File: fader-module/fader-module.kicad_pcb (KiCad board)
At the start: 2 copper layers, 33 parts, among them J1 Conn_1x05_Pin, J2 Conn_1x05_Socket, J7 Conn_01x06_Socket, SW1 1825910-6, SW2 1825910-6, U5 ATMEGA328P-AUR, U7 DRV8871DDAR

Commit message: fader begin route except i forgot widths anyways theyre mostly laid out the components i mean
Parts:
- moved C8 138.6 mm to (209.3, 90.4), turned to 90 degrees
- moved C7 138.5 mm to (209.2, 85.3), turned to -90 degrees
- moved R5 134.8 mm to (215.1, 90.7), turned to -90 degrees
- moved R4 134.8 mm to (215.1, 85.6), turned to -90 degrees
- moved C12 103.1 mm to (176.4, 107.9), turned to -90 degrees
- moved C13 100.7 mm to (176.3, 91.5), turned to -90 degrees
- moved R7 85.0 mm to (165.1, 86.7)
- moved R8 83.6 mm to (162.6, 110.3), turned to 90 degrees
- moved R9 83.1 mm to (163.3, 94.2), turned to 90 degrees
- moved C16 73.6 mm to (147.4, 111.8), turned to 180 degrees
- moved C6 72.2 mm to (142.9, 85.6), turned to 180 degrees
- moved SW1 70.0 mm to (170.0, 110.9)
- moved C11 67.3 mm to (142.6, 89.9), turned to 180 degrees
- moved SW2 65.7 mm to (170.2, 94.4)
- moved R14 61.6 mm to (143.5, 103.1), turned to 180 degrees
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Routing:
- net GND: track 0.00 -> 77.8 mm
- net +3V3: track 0.00 -> 52.5 mm
- net /MUTE: track 0.00 -> 14.9 mm
- net /SOLO: track 0.00 -> 14.1 mm
- net +9V: track 0.00 -> 12.3 mm
- net Net-(U5-PC0(ADC0/PCINT8)): track 0.00 -> 6.07 mm
- net Net-(U5-PC1(ADC1/PCINT9)): track 0.00 -> 5.93 mm
- net Net-(R15-Pad2): track 0.00 -> 4.26 mm
- net Net-(D2-A): track 0.00 -> 3.95 mm
- net Net-(U7-ILIM): track 0.00 -> 3.80 mm
- net Net-(D1-A): track 0.00 -> 3.79 mm
- net /TOUCH: track 0.00 -> 3.73 mm
- net Net-(R14-Pad2): track 0.00 -> 3.08 mm
- added copper zone on F.Cu, net GND

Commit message: HHHHAAAAHHHHH traces AHH
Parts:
- moved R17 8.60 mm to (102.0, 92.3)
- moved R3 7.18 mm to (93.8, 105.9)
- moved C14 7.14 mm to (101.1, 102.3), turned to -90 degrees
- moved C4 7.14 mm to (101.1, 97.0)
- moved C16 6.82 mm to (146.6, 105.0)
- moved R9 6.82 mm to (162.5, 87.5)
- moved SW2 6.82 mm to (169.4, 87.6)
- moved C13 6.82 mm to (175.5, 84.7)
- moved R14 6.82 mm to (142.7, 96.4)
- moved R16 6.82 mm to (133.9, 95.5)
- moved SW1 6.82 mm to (169.2, 104.1)
- moved U7 6.82 mm to (141.3, 90.1)
- moved C12 6.82 mm to (175.6, 101.2)
- moved J1 6.82 mm to (148.2, 108.3)
- moved R15 6.82 mm to (137.6, 96.4)
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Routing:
- net /MOSI: track 0.00 -> 45.5 mm
- net /MISO: track 0.00 -> 37.1 mm
- net /SCK: track 0.00 -> 33.2 mm
- net +3V3: track 52.5 -> 61.7 mm
- net GND: track 77.8 -> 72.0 mm
- net Net-(R15-Pad2): track 4.26 -> 2.74 mm
- net /TOUCH: track 3.73 -> 3.09 mm
- net +9V: track 12.3 -> 11.7 mm
- net (no net): vias 0 -> 1

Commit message: gotta add connector for motor prob LMAO
also do i need 9v caps??
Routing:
- net GND: track 72.0 -> 135.0 mm, vias 0 -> 2
- net Net-(P1-PadT): track 0.00 -> 61.9 mm, vias 0 -> 2
- net /SERVO: track 0.00 -> 59.0 mm
- net +3V3: track 61.7 -> 102.3 mm
- net /LINE: track 0.00 -> 35.3 mm

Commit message: i will combust
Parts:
- removed J7: Conn_01x06_Socket, Connector_IDC:IDC-Header_2x03_P2.54mm_Vertical
- removed P1: ~, PSM01:PSM01-081A_BRN
- added J3: Conn_01x02_Pin, TerminalBlock_Phoenix:TerminalBlock_Phoenix_MKDS-1,5-2-5.08_1x02_P5.08mm_Horizontal, F.Cu at (153.6, 88.3)
- added J4: Conn_01x06_Pin, Connector_IDC:IDC-Header_2x03_P2.54mm_Vertical, F.Cu at (182.4, 102.9)
- added J6: Conn_01x06_Pin, Connector_IDC:IDC-Header_2x03_P2.54mm_Vertical, F.Cu at (96.0, 83.7)
- D1, D2: footprint LED_SMD:LED_0805_2012Metric_Pad1.15x1.40mm_HandSolder -> Connector_Molex:Molex_KK-254_AE-6410-02A_1x02_P2.54mm_Vertical
- moved C7 24.7 mm to (183.9, 87.0), turned to 90 degrees
- moved C8 24.7 mm to (184.0, 91.9)
- moved R4 24.7 mm to (189.8, 87.1)
- moved R5 24.7 mm to (189.8, 92.1)
- moved J2 8.60 mm to (135.8, 38.9)
- moved R7 4.00 mm to (162.2, 82.8)
- moved C12 2.94 mm to (175.6, 104.1)
- moved R8 2.94 mm to (161.7, 106.5)
- moved R9 2.94 mm to (162.5, 90.4)
- moved SW1 2.94 mm to (169.2, 107.0)
- moved SW2 2.94 mm to (169.4, 90.5)
- moved C13 2.94 mm to (175.5, 87.6)
- moved D2 2.63 mm to (169.6, 82.8)
- moved R6 2.06 mm to (162.6, 99.4)
- moved R3 1.39 mm to (95.1, 106.5)
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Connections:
- R3 pad 2: Net-(P1-PadT) -> Net-(U5-PB2(PCINT2/~{SS}/OC1B))
- U5 pad 14: /TOUCH -> Net-(U5-PB2(PCINT2/~{SS}/OC1B))
- U7 pad 6: Net-(U7-OUT1) -> /A
- U7 pad 8: Net-(U7-OUT2) -> /B
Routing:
- net /SCL: track 0.00 -> 150.6 mm, vias 0 -> 1
- net GND: track 135.0 -> 280.0 mm, vias 2 -> 3
- net /SDA: track 0.00 -> 142.4 mm, vias 0 -> 1
- net /S_LED: track 0.00 -> 113.0 mm, vias 0 -> 2
- net +3V3: track 102.3 -> 204.8 mm, vias 0 -> 2
- net /SOLO: track 14.1 -> 111.8 mm, vias 0 -> 2
- net /MUTE: track 14.9 -> 105.7 mm
- net /M_LED: track 0.00 -> 83.2 mm
- net +9V: track 11.7 -> 81.9 mm, vias 0 -> 3
- net Net-(P1-PadT): track 61.9 -> 0.00 mm, vias 2 -> 0
- net /B: track 0.00 -> 48.7 mm
- net /SERVO: track 59.0 -> 19.7 mm
- net /MOTOR1: track 0.00 -> 35.4 mm
- net /MOTOR2: track 0.00 -> 31.4 mm
- net /A: track 0.00 -> 13.5 mm
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
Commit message: eRrOr FrOnT sOlDeR mAsK
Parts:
- moved C9 33.2 mm to (118.4, 109.2)
- moved J6 33.2 mm to (128.3, 91.0)
- moved R17 33.2 mm to (134.3, 99.3)
- moved R3 33.2 mm to (127.4, 113.8)
- moved U5 33.2 mm to (126.1, 106.1)
- moved C10 33.2 mm to (118.6, 104.8)
- moved C14 33.2 mm to (133.4, 109.6)
- moved C4 33.2 mm to (133.4, 104.3)
- moved J2 28.5 mm to (160.0, 53.9)
- moved J4 20.0 mm to (201.0, 110.2)
- moved R8 18.7 mm to (179.0, 113.6)
- moved C7 18.3 mm to (199.6, 96.3)
- moved C8 18.3 mm to (199.7, 101.1)
- moved R4 18.3 mm to (205.5, 96.3)
- moved R5 18.3 mm to (205.5, 101.4)
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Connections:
- U7 pad 10: (no net) -> GND
- U7 pad 11: (no net) -> GND
- U7 pad 12: (no net) -> GND
- U7 pad 13: (no net) -> GND
- U7 pad 14: (no net) -> GND
- U7 pad 15: (no net) -> GND
- U7 pad 16: (no net) -> GND
- U7 pad 17: (no net) -> GND
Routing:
- net /TOUCH: track 0.00 -> 82.9 mm, vias 0 -> 2
- net Net-(U5-PC1(ADC1/PCINT9)): track 8.27 -> 84.1 mm, vias 0 -> 2
- net Net-(U5-PC0(ADC0/PCINT8)): track 11.2 -> 84.5 mm
- net +3V3: track 204.8 -> 247.2 mm, vias 2 -> 3
- net /SCL: track 150.6 -> 116.6 mm
- net /MOTOR1: track 35.4 -> 69.2 mm, vias 0 -> 2
- net /MOTOR2: track 31.4 -> 63.3 mm, vias 0 -> 2
- net /S_LED: track 113.0 -> 81.7 mm
- net /B: track 48.7 -> 19.0 mm
- net /SDA: track 142.4 -> 113.2 mm
- net /MUTE: track 105.7 -> 77.5 mm
- net GND: track 280.0 -> 303.1 mm, vias 3 -> 5
- net /M_LED: track 83.2 -> 60.1 mm
- net /SOLO: track 111.8 -> 96.9 mm
- net /SCK: track 33.2 -> 27.7 mm, vias 0 -> 1
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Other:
- board outline added: 100 x 75 mm

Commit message: done w pcb gerbert time
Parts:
- moved C9 66.4 mm to (142.8, 47.5), turned to 180 degrees
- moved R5 64.1 mm to (150.7, 134.6), turned to 180 degrees
- moved C10 63.9 mm to (147.3, 47.7), turned to 0 degrees
- moved R4 62.8 mm to (155.7, 134.6), turned to 180 degrees
- moved J4 62.5 mm to (141.8, 130.1), turned to -90 degrees
- moved R3 58.3 mm to (138.2, 56.5), turned to 90 degrees
- moved C8 56.1 mm to (150.9, 128.8), turned to 0 degrees
- moved U5 54.7 mm to (145.9, 55.1), turned to -90 degrees
- moved C7 54.5 mm to (155.8, 128.7), turned to 0 degrees
- moved C12 52.9 mm to (138.5, 120.1), turned to 180 degrees
- moved J2 51.9 mm to (198.2, 89.1), turned to -90 degrees
- moved SW1 47.9 mm to (137.1, 114.1), turned to -90 degrees
- moved C14 47.9 mm to (142.5, 62.5), turned to 180 degrees
- moved J6 46.9 mm to (161.0, 57.4), turned to 180 degrees
- moved C4 44.2 mm to (147.7, 62.5), turned to 0 degrees
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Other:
- board size 100 x 75 mm -> 75 x 100 mm
- rule pad_to_mask_clearance: 0 -> 0.05
- board text added: "Desktop Audio Panel Fader Module v1 Project No. 85"

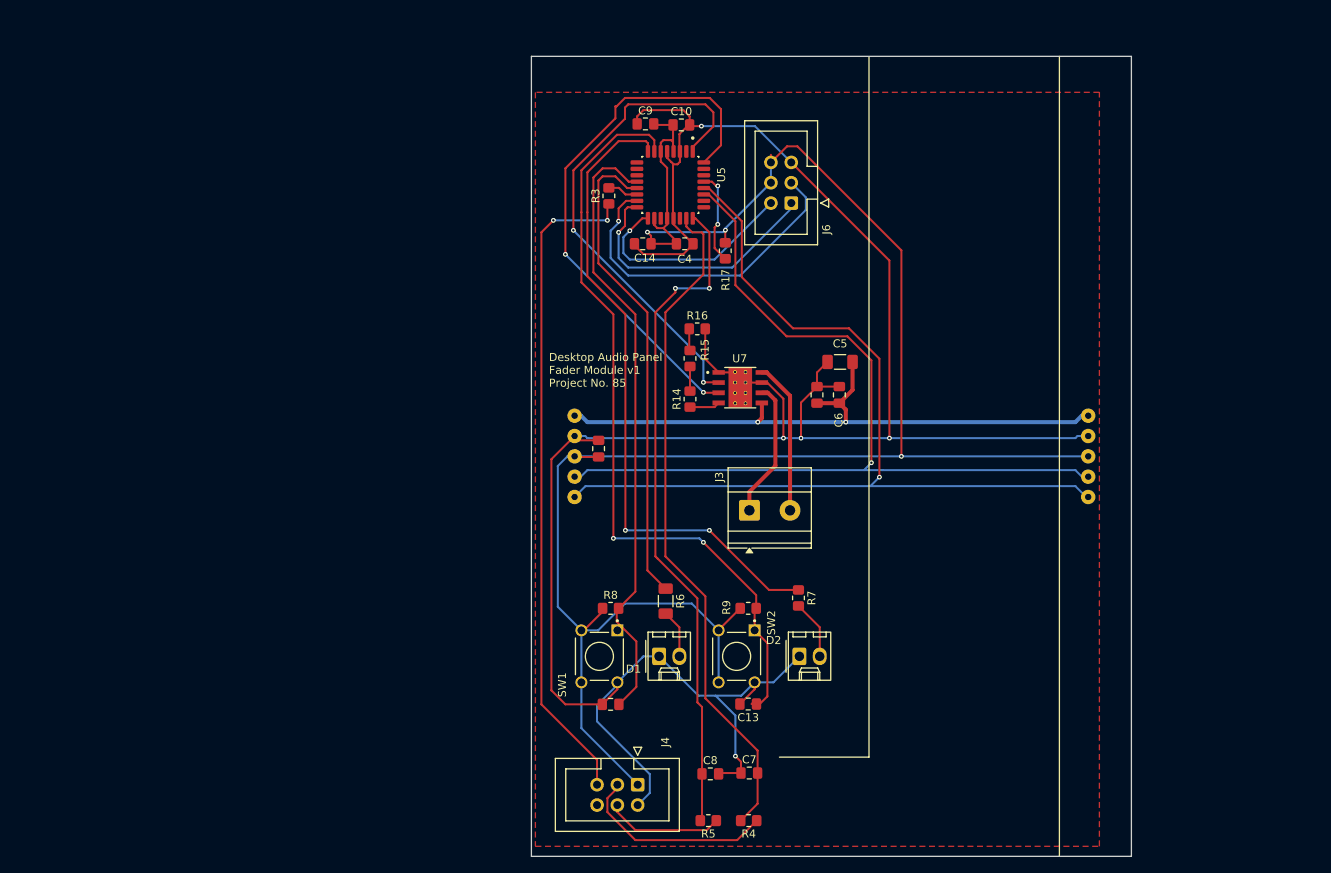
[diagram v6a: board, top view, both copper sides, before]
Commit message: the fuckin u7 clearance is acting up again
i also forgot how to wire a button LOL
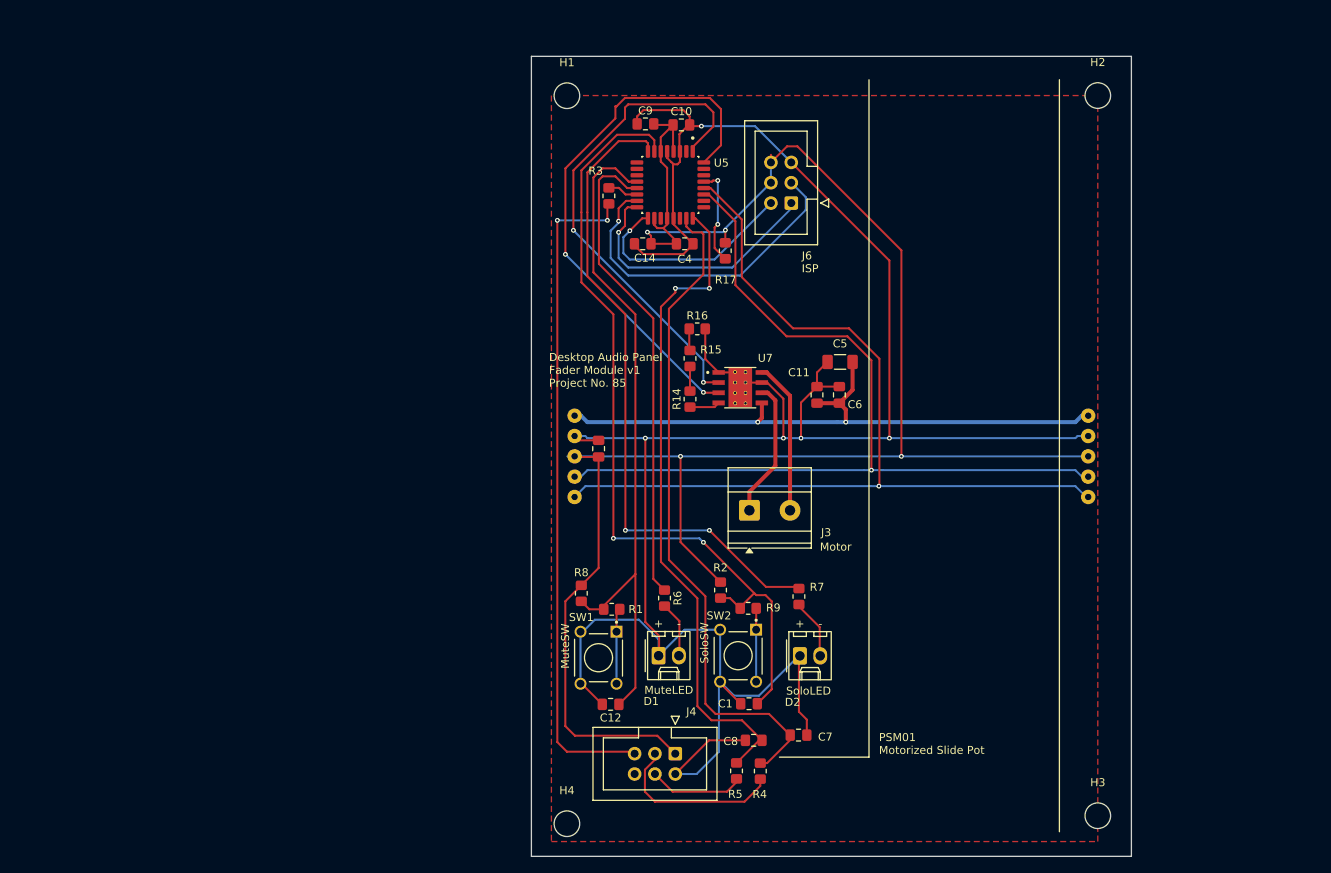
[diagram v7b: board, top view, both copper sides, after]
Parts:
- removed C13: 0.1uF, Capacitor_SMD:C_0805_2012Metric_Pad1.18x1.45mm_HandSolder
- added C1: 1uF, Capacitor_SMD:C_0805_2012Metric_Pad1.18x1.45mm_HandSolder, F.Cu at (155.8, 120.0)
- added H1: MountingHole, MountingHole:MountingHole_3.2mm_M3, F.Cu at (133.0, 44.0)
- added H2: MountingHole, MountingHole:MountingHole_3.2mm_M3, F.Cu at (199.4, 44.0)
- added H3: MountingHole, MountingHole:MountingHole_3.2mm_M3, F.Cu at (199.4, 134.0)
- added H4: MountingHole, MountingHole:MountingHole_3.2mm_M3, F.Cu at (133.0, 135.0)
- added R1: 10k, Resistor_SMD:R_0805_2012Metric_Pad1.20x1.40mm_HandSolder, F.Cu at (138.6, 108.2)
- added R2: 10k, Resistor_SMD:R_0805_2012Metric_Pad1.20x1.40mm_HandSolder, F.Cu at (152.2, 105.8)
- C12: value 0.1uF -> 1uF
- R6: value 330 -> 1k; footprint Capacitor_SMD:C_1206_3216Metric_Pad1.33x1.80mm_HandSolder -> Resistor_SMD:R_0805_2012Metric_Pad1.20x1.40mm_HandSolder
- R7: value 330 -> 1k
- moved C7 7.77 mm to (161.9, 123.9), turned to 180 degrees
- moved R5 7.14 mm to (154.2, 128.4), turned to 90 degrees
- moved C8 6.86 mm to (156.3, 124.6), turned to 180 degrees
- moved R4 6.36 mm to (157.2, 128.4), turned to 90 degrees
- moved J4 6.09 mm to (146.5, 126.2)
- moved R8 4.11 mm to (134.8, 106.2), turned to -90 degrees
- moved R6 0.41 mm to (145.2, 106.8)
- moved SW2 0.20 mm to (154.4, 114.0)
- moved SW1 0.20 mm to (136.9, 114.2)
- moved R7 0.19 mm to (162.0, 106.6)
- moved D1 0.10 mm to (144.5, 114.0)
- moved D2 0.09 mm to (162.1, 114.0)
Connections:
- R9 pad 1: +3V3 -> /SOLO
- R9 pad 2: /SOLO -> Net-(R9-Pad2)
- SW1 pad 1: /MUTE -> Net-(R1-Pad2)
- SW1 pad 2: GND -> Net-(R1-Pad2)
- SW1 pad 3: +3V3 -> GND
- SW1 pad 4: +3V3 -> GND
- SW2 pad 1: /SOLO -> Net-(R9-Pad2)
- SW2 pad 2: GND -> Net-(R9-Pad2)
- SW2 pad 3: +3V3 -> GND
- SW2 pad 4: +3V3 -> GND
- U7 pad 10: GND -> (no net)
- U7 pad 11: GND -> (no net)
- U7 pad 12: GND -> (no net)
- U7 pad 13: GND -> (no net)
- U7 pad 14: GND -> (no net)
- U7 pad 15: GND -> (no net)
- U7 pad 16: GND -> (no net)
- U7 pad 17: GND -> (no net)
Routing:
- net GND: track 303.1 -> 313.9 mm
- net +3V3: track 247.2 -> 237.4 mm, vias 3 -> 4
- net Net-(R1-Pad2): track 0.00 -> 9.47 mm
- net Net-(R9-Pad2): track 0.00 -> 9.25 mm
- net /MUTE: track 77.5 -> 84.7 mm
- net /SOLO: track 96.9 -> 102.5 mm
- net /LINE: track 25.1 -> 21.9 mm
- net /SERVO: track 14.7 -> 12.0 mm
- net Net-(D1-A): track 6.05 -> 7.05 mm
- net Net-(U5-PC1(ADC1/PCINT9)): track 84.1 -> 83.1 mm
- net /TOUCH: track 82.9 -> 83.9 mm
- net Net-(U5-PC0(ADC0/PCINT8)): track 84.5 -> 83.7 mm
- net Net-(U5-PC6(~{RESET}/PCINT14)): track 11.8 -> 12.3 mm
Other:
- board text added: "PSM01 Motorized Slide Pot"
